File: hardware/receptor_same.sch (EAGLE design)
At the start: 16 parts, among them J1 ICSP, J2 SERIAL, U1 ATMEGA328P_TQFP, U2 SI4707, Y1 8MHz, Y2 3.2768KHZ

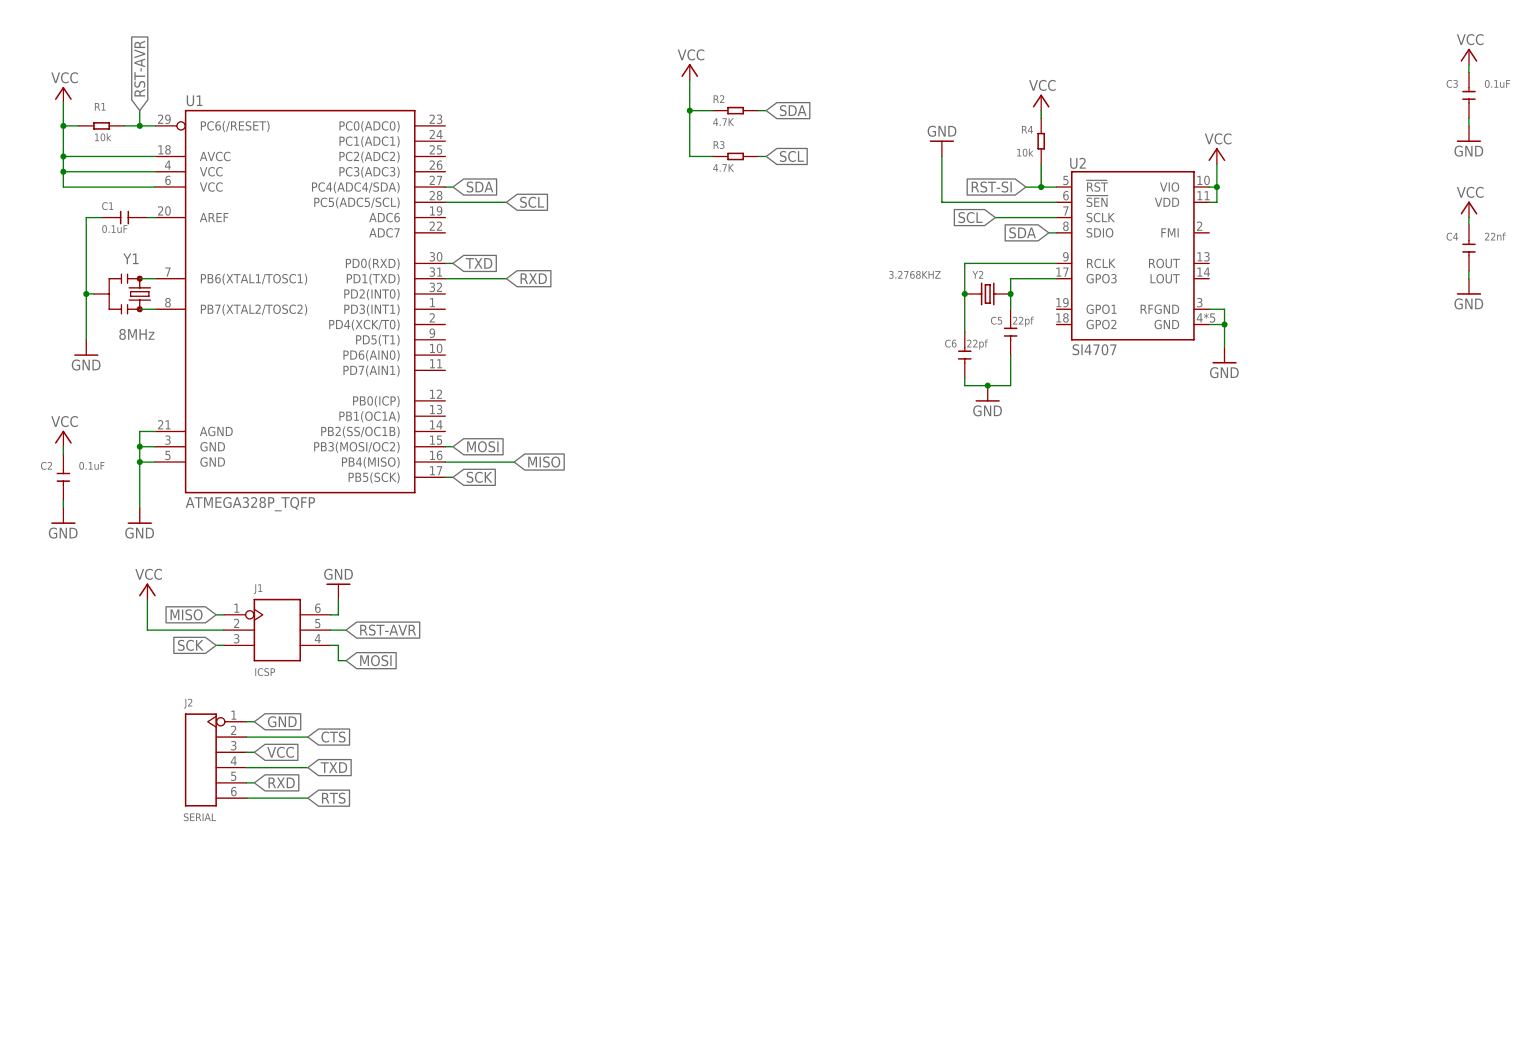
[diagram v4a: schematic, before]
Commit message: terminamos si4707, tda611, io, gpio y leds
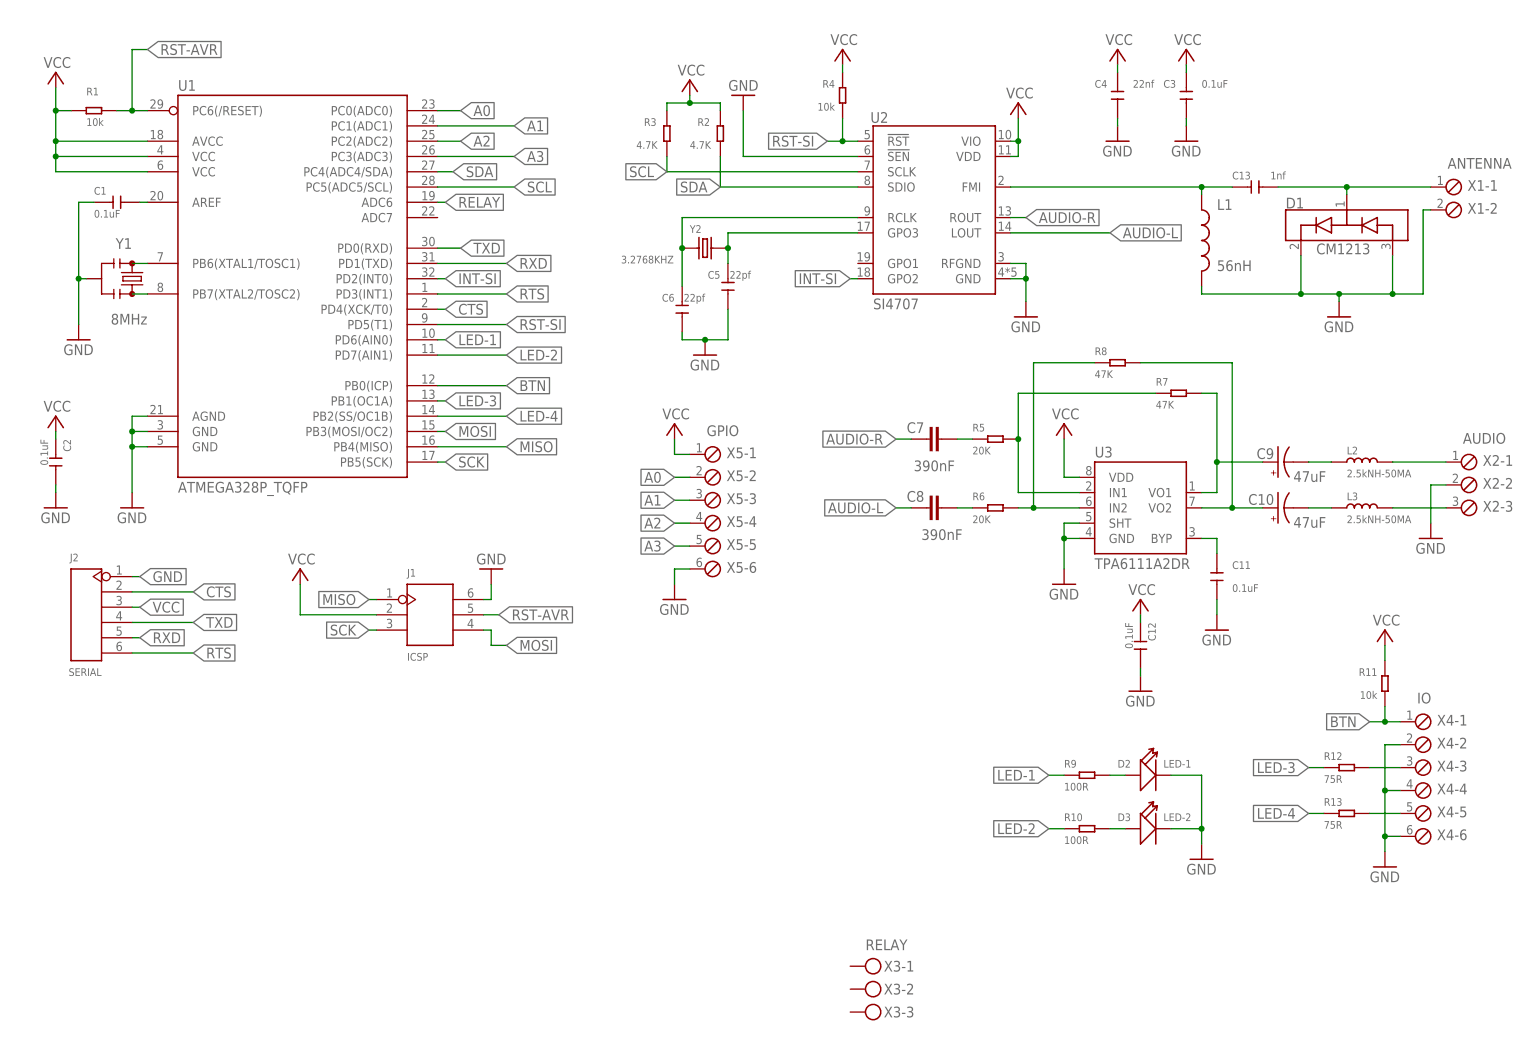
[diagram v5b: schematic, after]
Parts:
- added C10, C9: 47uF, SparkFun-Capacitors:47UF-POLAR-EIA3528-10V-10%
- added C11, C12: 0.1uF, OPL_Capacitor:CERAMIC-100NF-50V-10%-X7R(0603)
- added C13: 1nf, OPL_Capacitor:CERAMIC-1NF-50V-5%-C0G(0603)
- added C7, C8: 390nF, SparkFun-Capacitors:390NF-0603-10V-10%
- added D1: CM1213, sparkfun_si4707_breakout:SPARKFUN-DISCRETESEMI_CM1213
- added D2: LED-1, OPL_Optoelectronics:SMD-LED-CLEAR-GREEN(0805)
- added D3: LED-2, OPL_Optoelectronics:SMD-LED-CLEAR-GREEN(0805)
- added L1: 56nH, sparkfun_si4707_breakout:SPARKFUN-PASSIVES_INDUCTOR0603
- added L2, L3: 2.5kNH-50MA, OPL_Inductor:SMD-INDUCTOR-4.7NH-0.3NH-300MA(0402)
- added R10, R9: 100R, OPL_Resistor:SMD-RES-100R-5%-1/10W(0603)
- added R11: 10k, OPL_Resistor:SMD-RES-10K-5%-1/10W(0603)
- added R12, R13: 75R, OPL_Resistor:SMD-RES-75R-5%-1/10W(0603)
- added R5, R6: 20K, OPL_Resistor:SMD-RES-20K-1%-1/10W(0603)
- added R7, R8: 47K, OPL_Resistor:SMD-RES-47K-5%-1/10W(0603)
- added U3: TPA6111A2DR, SparkFun-IC-Amplifiers:TPA6111SMD-T
- added X1: ANTENNA, con-phoenix-254:MPT2
- added X2: AUDIO, con-phoenix-254:MPT3
- added X3: RELAY, con-phoenix-508:MKDSN1,5/3-5,08
- added X4: IO, con-phoenix-254:MPT6
- added X5: GPIO, con-phoenix-254:MPT6
- C5, C6: SPICEPREFIX (none) -> C
- J2, U2: SPICEPREFIX (none) -> X
- R4: SPICEPREFIX (none) -> R
- Y2: SPICEPREFIX (none) -> B
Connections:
- new net A0: U1.PC0(ADC0), X5-2.1
- new net A1: U1.PC1(ADC1), X5-3.1
- new net A2: U1.PC2(ADC2), X5-4.1
- new net A3: U1.PC3(ADC3), X5-5.1
- new net AUDIO-L: C8.1, U2.LOUT
- new net AUDIO-R: C7.1, U2.ROUT
- new net BTN: R11.2, U1.PB0(ICP), X4-1.1
- new net INT-SI: U1.PD2(INT0), U2.GPO2
- new net LED-1: R9.1, U1.PD6(AIN0)
- new net LED-2: R10.1, U1.PD7(AIN1)
- new net LED-3: R12.1, U1.PB1(OC1A)
- new net LED-4: R13.1, U1.PB2(SS/OC1B)
- new net N$10: R5.2, R7.1, U3.IN1
- new net N$11: C9.+, R7.2, U3.VO1
- new net N$12: R6.2, R8.1, U3.IN2
- new net N$13: C10.+, R8.2, U3.VO2
- new net N$14: C9.-, L2.1
- new net N$15: L2.2, X2-1.1
- new net N$16: L3.2, X2-3.1
- new net N$17: C10.-, L3.1
- new net N$18: R12.2, X4-3.1
- new net N$19: D3.+, R10.2
- new net N$20: D2.+, R9.2
- new net N$21: R13.2, X4-5.1
- new net N$22: C13.2, D1.CH1, X1-1.1
- new net N$6: C13.1, L1.1, U2.FMI
- new net N$7: C7.2, R5.1
- new net N$8: C8.2, R6.1
- new net N$9: C11.1, U3.BYP
- new net RELAY: U1.ADC6
- net CTS: now also U1.PD4(XCK/T0)
- net GND: now also C11.2, C12.2, D1.VN, D1.VP, D2.-, D3.-, L1.2, U3.GND, U3.SHT, X1-2.1, X2-2.1, X4-2.1, X4-4.1, X4-6.1, X5-6.1
- net RST-SI: now also U1.PD5(T1)
- net RTS: now also U1.PD3(INT1)
- net VCC: now also C12.1, R11.1, U3.VDD, X5-1.1
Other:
- moved on the sheet: C1, C2, C3, C4, C5, C6, J1, J2, R1, R2, R3, R4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

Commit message: fuente de poder
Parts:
- added C14: 10UF-50V, OPL_Capacitor:CERAMIC-10UF-25V-10%-X5R(1206)
- added C15: 100nf-50V, OPL_Capacitor:CERAMIC-100NF-50V-10%-X7R(0603)
- added C16, C17: 10UF-6.3V, OPL_Capacitor:CERAMIC-10UF-6.3V-20%-X5R(0603)
- added C18: 0.1uF, OPL_Capacitor:CERAMIC-100NF-50V-10%-X7R(0603)
- added D4: MMSD4148, OPL_Discrete_Semiconductor:SMD-DIODE-100V-200MA(SOD-123)
- added D5: 40V-1A, OPL_Discrete_Semiconductor:SMD-DIODE-SCHOTTKY-40V-1A(DO-214AC)
- added J3: GPIO, OPL_Connector:DIP-BLACK-MALE-HEADER-VERT(8P-2.54)
- added L4: 22UH-2.2A, seed-opl-2017-01-inductor-akita:303010525_22UH_7.1X6.6MM
- added R14: 52.3K, OPL_Resistor:SMD-RES-51K-5%-1/10W(0603)
- added R15: 10K, OPL_Resistor:SMD-RES-10K-5%-1/10W(0603)
- added U4: MCP16301/H, mcp16301:MCP16301/H
- added U5: TLV70233DBVR, mf_ic_power:TLV70233PDBVR
- C10, C11, C12, C3, C7, C8, C9: SPICEPREFIX (none) -> C
- L2, L3: SPICEPREFIX (none) -> L
- R5, R6, R7, R8: SPICEPREFIX (none) -> R
- U3, X2: SPICEPREFIX (none) -> X
- X5: value GPIO -> POWER; device con-phoenix-254:MPT6 -> con-phoenix-254:MPT2; MPN 1725698 -> 1725656
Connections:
- removed net VCC: C12.1, C2.1, C3.1, C4.1, J1.2, J2.3, R1.2, R11.1, R2.1, R3.1, R4.1, U1.AVCC, U1.VCC@4, U1.VCC@6, U2.VDD, U2.VIO, U3.VDD, X5-1.1
- new net +3V3: C12.1, C18.1, C2.1, C3.1, C4.1, J1.2, J2.3, J3.2, R1.2, R11.1, R2.1, R3.1, R4.1, U1.AVCC, U1.VCC@4, U1.VCC@6, U2.VDD, U2.VIO, U3.VDD, U5.VOUT
- new net +5V: C16.2, C17.2, D4.+, J3.1, L4.P$2, R14.2, U5.EN, U5.VIN
- new net A6: J3.7, U1.ADC6
- new net N$23: C15.1, D5.-, L4.P$1, U4.SW
- new net N$24: C15.2, D4.-, U4.BOOST
- new net N$25: C14.2, U4.EN, U4.VIN, X5-1.1
- new net N$27: R14.1, R15.1, U4.VFB
- net A0: now also J3.3; no longer X5-2.1
- net A1: now also J3.4; no longer X5-3.1
- net A2: now also J3.5; no longer X5-4.1
- net A3: now also J3.6; no longer X5-5.1
- net GND: now also C14.1, C16.1, C17.1, C18.2, D5.+, J3.8, R15.2, U4.GND, U5.GND/ADJ, X5-2.1; no longer X5-6.1
- net RELAY: now also U1.ADC7; no longer U1.ADC6
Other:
- moved on the sheet: C10, C11, C12, C13, C3, C4, C5, C6, C7, C8, C9, D1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

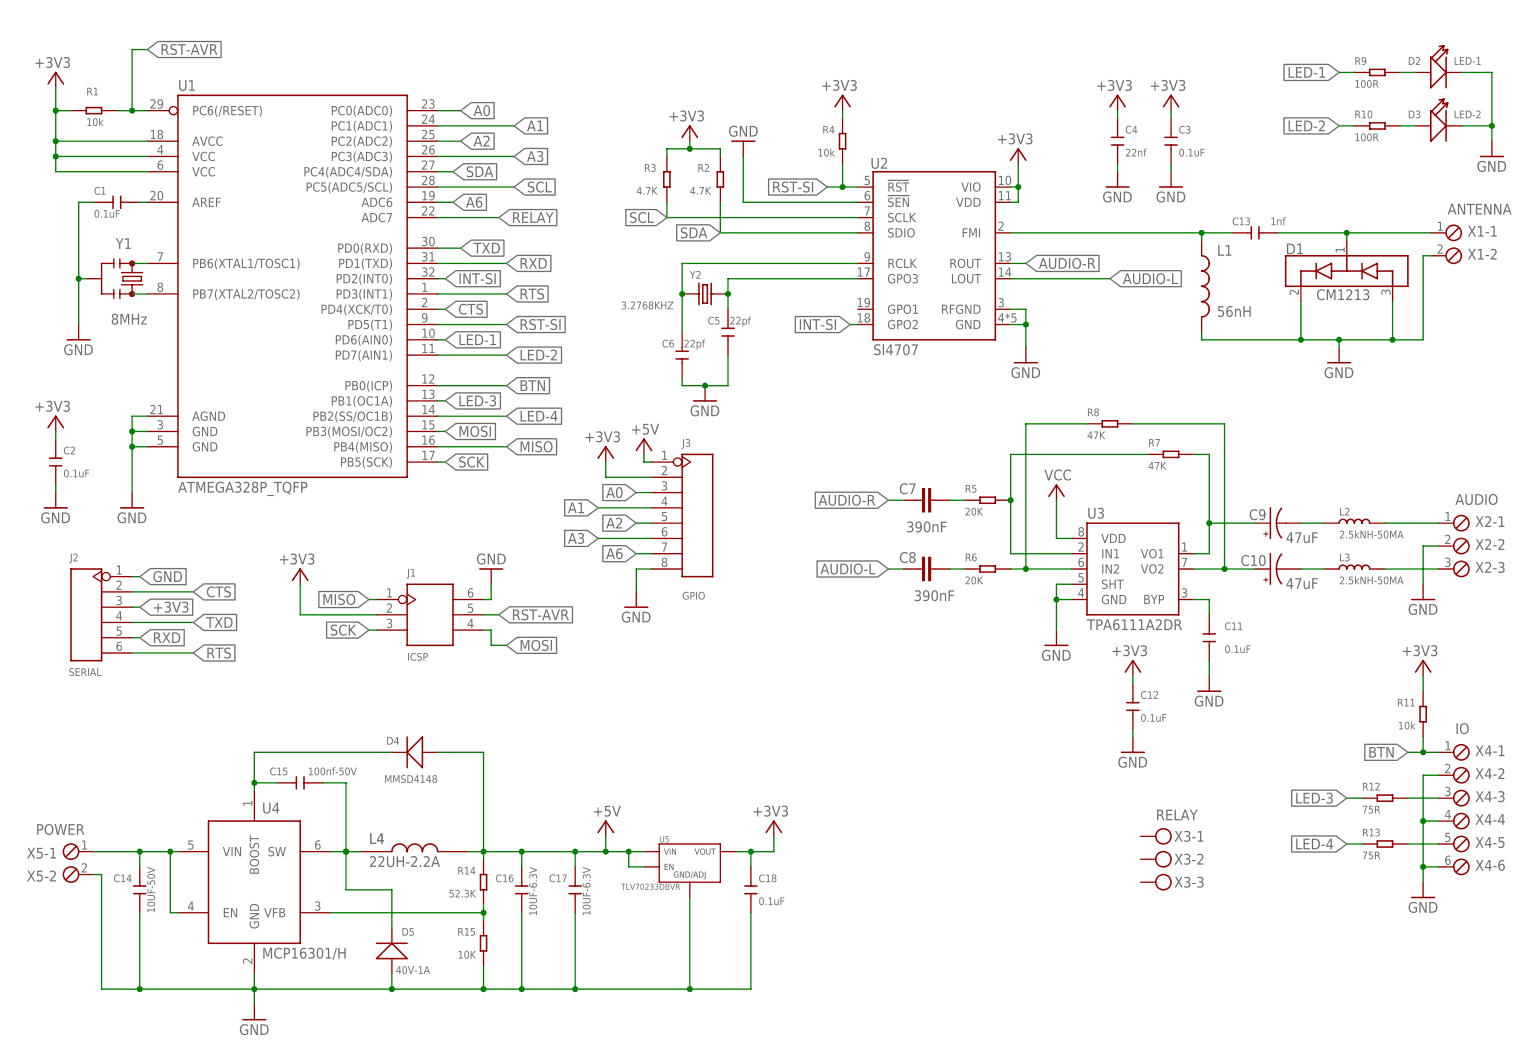
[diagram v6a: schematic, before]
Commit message: 120 para resistencias de leds (12.5 mA)
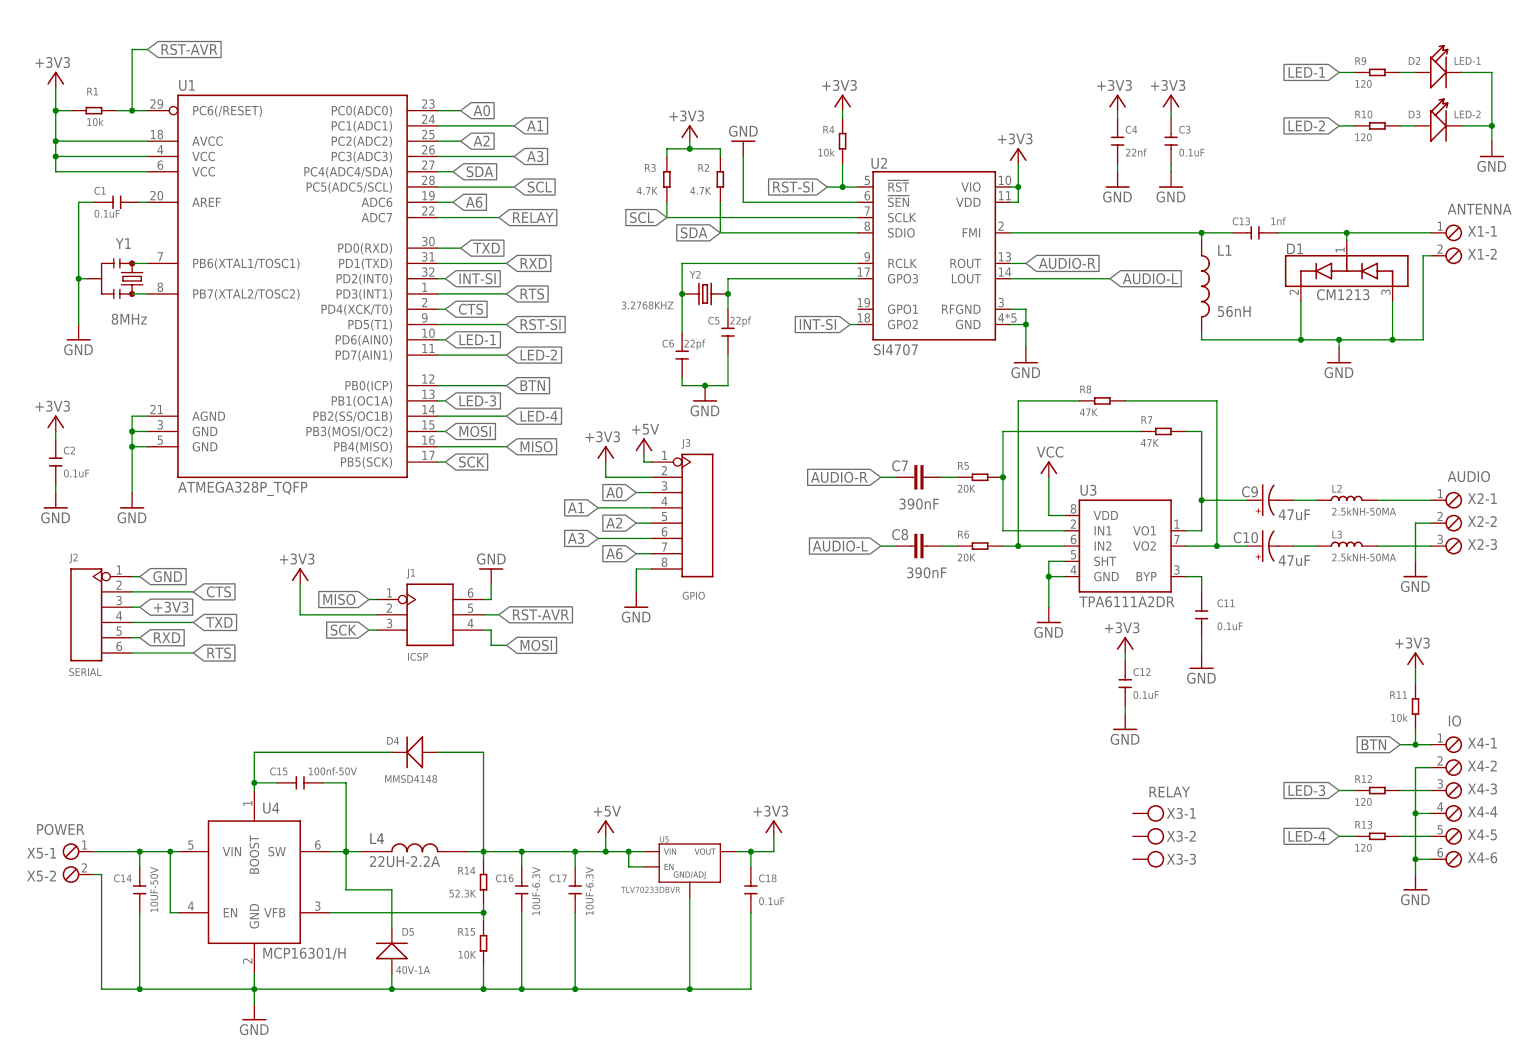
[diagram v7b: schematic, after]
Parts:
- R10, R9: value 100R -> 120; device OPL_Resistor:SMD-RES-100R-5%-1/10W(0603) -> OPL_Resistor:SMD-RES-120R-5%-1/8W(0805); MPN (none) -> RC0805JR-07120RL
- R12, R13: value 75R -> 120; device OPL_Resistor:SMD-RES-75R-5%-1/10W(0603) -> OPL_Resistor:SMD-RES-120R-5%-1/8W(0805); MPN RC0603JR-0775RL -> RC0805JR-07120RL
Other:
- moved on the sheet: C10, C11, C12, C7, C8, C9, L2, L3, R11, R12, R13, R5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

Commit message: segunda hoja: relay y aux power
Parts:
- added D6: MMSD4148, OPL_Discrete_Semiconductor:SMD-DIODE-100V-200MA(SOD-123)
- added J4: AUX-POWER, OPL_Connector:DIP-BLACK-MALE-HEADER-VERT(3P-2.54)
- added K1: (no value), OPL_Relay:RELAY-HLS8L-DC5V-S-CHLS8L-DC5V-S-C
- added Q1: MMBT3904LT1G, OPL_Discrete_Semiconductor:SMD-TRANSISTORS-NPN-40V-200MA-MMBT3904LT1G(SOT-23)
- added R16: 1.5K, OPL_Resistor:SMD-RES-1.5K-5%-1/10W(0603)
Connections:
- new net N$26: K1.COM, X3-2.KL
- new net N$28: K1.NO, X3-1.KL
- new net N$29: K1.NC, X3-3.KL
- new net N$30: D6.-, K1.V-, Q1.C
- new net N$31: Q1.B, R16.2
- net +3V3: now also J4.P$1
- net +5V: now also D6.+, J4.P$3, K1.V+
- net BTN: now also U1.PB2(SS/OC1B); no longer U1.PB0(ICP)
- net GND: now also J4.P$2, Q1.E
- net LED-3: now also U1.PB0(ICP); no longer U1.PB1(OC1A)
- net LED-4: now also U1.PB1(OC1A); no longer U1.PB2(SS/OC1B)
- net RELAY: now also R16.1
